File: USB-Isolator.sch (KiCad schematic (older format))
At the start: 8 parts, among them U5 ADUM3160

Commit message: Mäusepiano (for Piano-Beginner) Areas tidied up new Phase- and Batterie-Connector and Benchmark for Pressfit Hall-filter back on PCB solder-jumper for choice: Resolver or Hallfilter
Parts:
- added R11: 1Meg, Resistors_SMD:R_0805, symbol Amalga_100-rescue:R-Device
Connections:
- wire segments 39 -> 42
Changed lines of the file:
@@
 GND1
 Wire Wire Line
-	2500 3850 2500 3550
+	2500 3850 2500 3750
 Wire Wire Line
 	2500 3550 2950 3550
@@
 Wire Wire Line
 	3650 2800 4050 2800
+Wire Wire Line
+	2950 3750 3250 3750
+$Comp
+L Amalga_100-rescue:R-Device R?
+U 1 1 5CB7CEF0
+P 2800 3750
+AR Path="/5CB7CEF0" Ref="R?"  Part="1"
+AR Path="/5CB8FAD2/5CB7CEF0" Ref="R11"  Part="1"
+F 0 "R11" V 2880 3750 50  0000 C CNN
+F 1 "1Meg" V 2800 3750 50  0000 C CNN
+F 2 "Resistors_SMD:R_0805" V 2730 3750 30  0001 C CNN
+F 3 "" H 2800 3750 30  0000 C CNN
+	1    2800 3750
+	0    1    1    0
+$EndComp
+Connection ~ 3250 3750
+Wire Wire Line
+	2650 3750 2500 3750
+Connection ~ 2500 3750
+Wire Wire Line
+	2500 3750 2500 3550
 $EndSCHEMATC

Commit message: -tidied up resolver circuit (need voltage detection on reset pin. >10µs, low active)
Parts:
- U5: symbol Interface_USB:ADUM3160 -> Amalga_100-rescue:ADUM3160-Interface_USB
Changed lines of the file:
@@
 EESchema Schematic File Version 4
 LIBS:Amalga_100-cache
-EELAYER 26 0
+EELAYER 29 0
 EELAYER END
 $Descr A4 11693 8268
@@
 	3350 3850 3350 3750
 $Comp
-L Interface_USB:ADUM3160 U?
+L Amalga_100-rescue:ADUM3160-Interface_USB U?
 U 1 1 5CB9A61A
 P 3150 2800

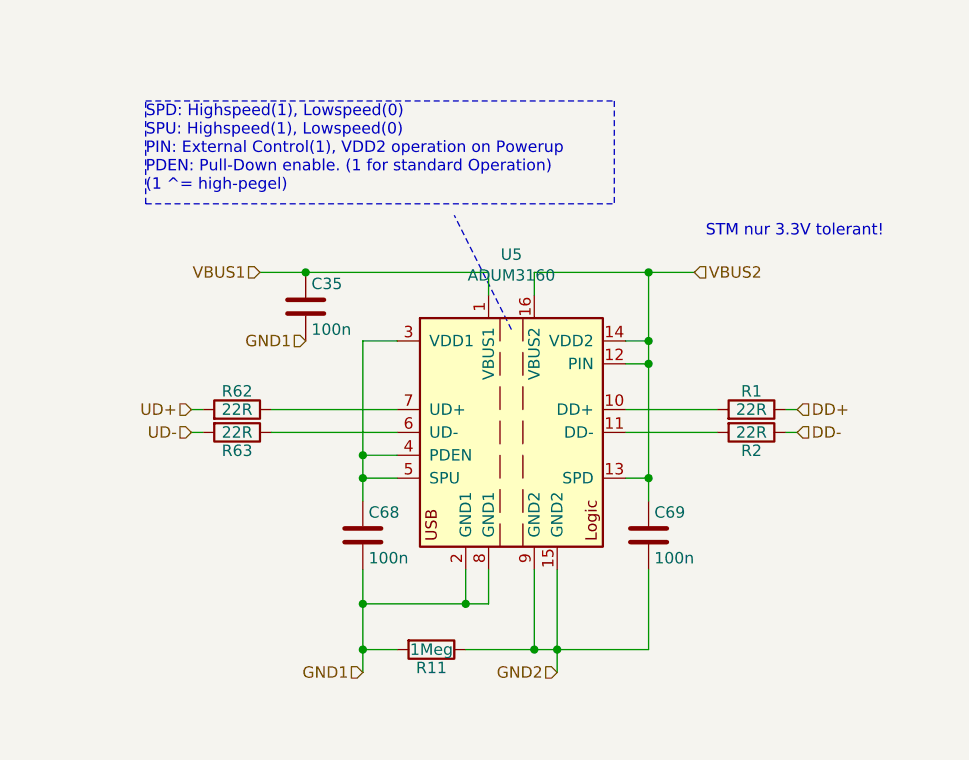
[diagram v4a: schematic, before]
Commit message: activated pulldown res on usb-Isolator IC
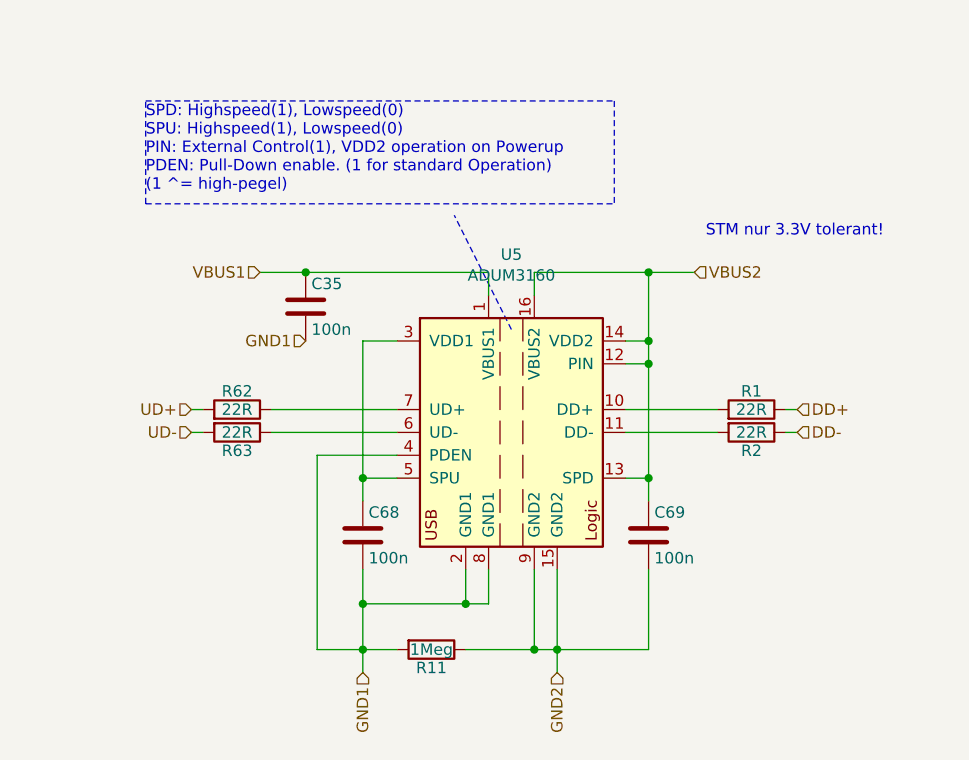
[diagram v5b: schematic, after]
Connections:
- net GND1: now also U5.4 (PDEN)
- net at C68.1, U5.3 (VDD1), U5.5 (SPU): no longer U5.4 (PDEN)
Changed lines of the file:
@@
 EESchema Schematic File Version 4
 LIBS:Amalga_100-cache
-EELAYER 26 0
+EELAYER 29 0
 EELAYER END
 $Descr A4 11693 8268
@@
 	3050 2100 3050 2200
 Wire Wire Line
-	2650 2900 2500 2900
-Wire Wire Line
-	2500 2900 2500 2400
-Wire Wire Line
 	2500 2400 2650 2400
 Text Notes 1550 1750 0    50   ~ 0
@@
 Wire Wire Line
 	3750 3000 3750 2500
-Wire Wire Line
-	2500 3000 2500 2900
-Connection ~ 2500 2900
 Wire Wire Line
 	2500 3400 2500 3550
@@
 Text HLabel 4400 2800 2    50   Input ~ 0
 DD-
-Text HLabel 3350 3850 0    50   Input ~ 0
+Text HLabel 3350 3850 3    50   Input ~ 0
 GND2
-Text HLabel 2500 3850 0    50   Input ~ 0
+Text HLabel 2500 3850 3    50   Input ~ 0
 GND1
 Wire Wire Line
@@
 $EndComp
 Connection ~ 3250 3750
+Connection ~ 2500 3750
+Wire Wire Line
+	2500 3750 2500 3550
+Wire Wire Line
+	2500 2400 2500 3000
 Wire Wire Line
 	2650 3750 2500 3750
-Connection ~ 2500 3750
-Wire Wire Line
-	2500 3750 2500 3550
+Wire Wire Line
+	2650 2900 2300 2900
+Wire Wire Line
+	2300 2900 2300 3750
+Wire Wire Line
+	2300 3750 2500 3750
 $EndSCHEMATC

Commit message: -changed wrong pin-header (swd)
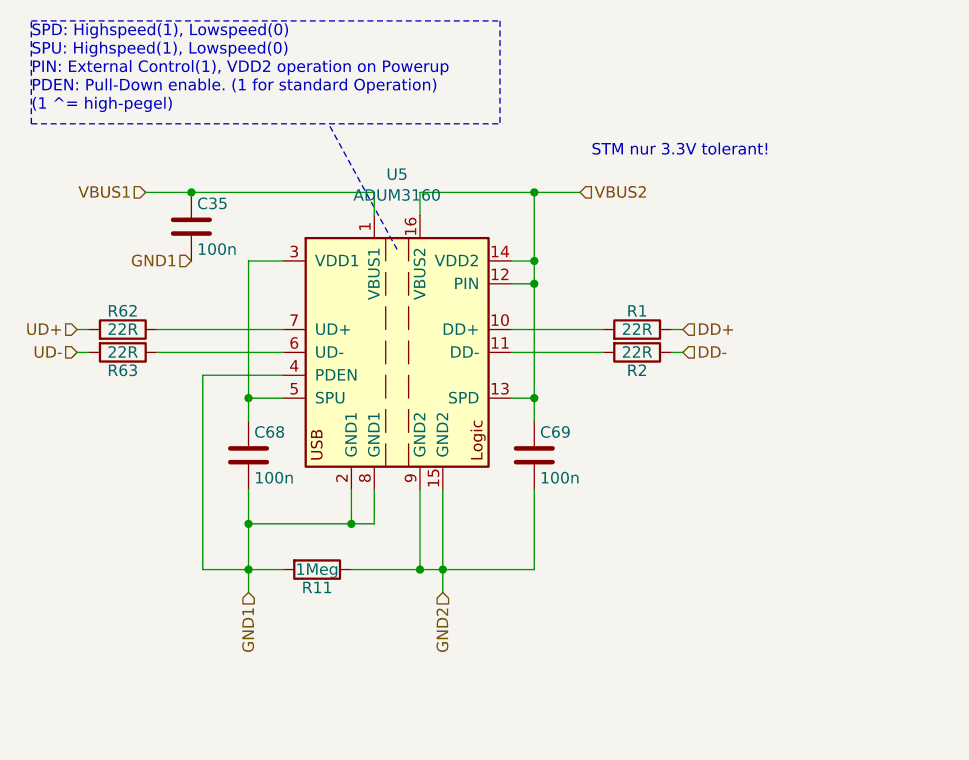
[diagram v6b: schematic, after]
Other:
- moved on the sheet: C35, C68, C69, R1, R11, R2, R62, R63, U5

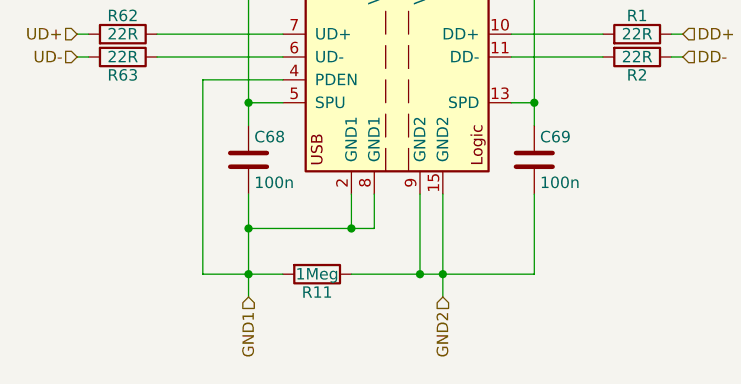
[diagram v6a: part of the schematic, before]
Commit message: -changed ad2s1200 to ad2s1205  (pin compatibel) -changed excitation-buffer circuit. (AD8397 in use now) -fixed thermal-connections of planes
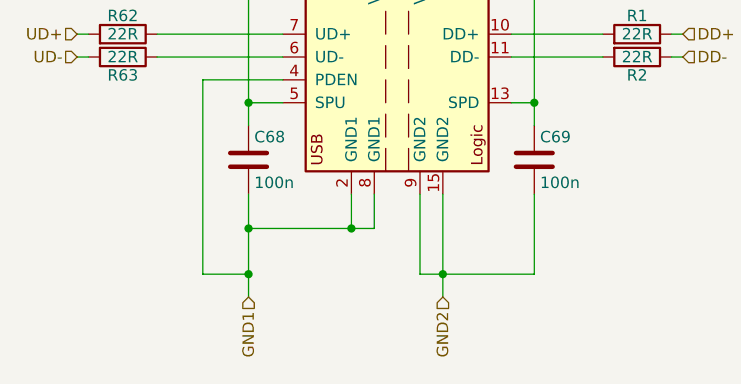
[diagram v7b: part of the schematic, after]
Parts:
- removed R11: 1Meg, Resistors_SMD:R_0805, symbol Amalga_100-rescue:R-Device
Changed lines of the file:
@@
 EESchema Schematic File Version 4
 LIBS:Amalga_100-cache
-EELAYER 26 0
+EELAYER 29 0
 EELAYER END
 $Descr A4 11693 8268
@@
 Wire Wire Line
 	3150 2450 3550 2450
-Wire Wire Line
-	2450 3400 2750 3400
-$Comp
-L Amalga_100-rescue:R-Device R?
-U 1 1 5CB7CEF0
-P 2300 3400
-AR Path="/5CB7CEF0" Ref="R?"  Part="1"
-AR Path="/5CB8FAD2/5CB7CEF0" Ref="R11"  Part="1"
-F 0 "R11" V 2380 3400 50  0000 C CNN
-F 1 "1Meg" V 2300 3400 50  0000 C CNN
-F 2 "Resistors_SMD:R_0805" V 2230 3400 30  0001 C CNN
-F 3 "" H 2300 3400 30  0000 C CNN
-	1    2300 3400
-	0    1    1    0
-$EndComp
-Connection ~ 2750 3400
 Connection ~ 2000 3400
 Wire Wire Line
@@
 	2000 2050 2000 2650
 Wire Wire Line
-	2150 3400 2000 3400
-Wire Wire Line
 	2150 2550 1800 2550
